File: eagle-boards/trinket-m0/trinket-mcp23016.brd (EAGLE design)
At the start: 60 x 41.6 mm, 10 parts, among them IC1 MCP23016P, Q1 BC547

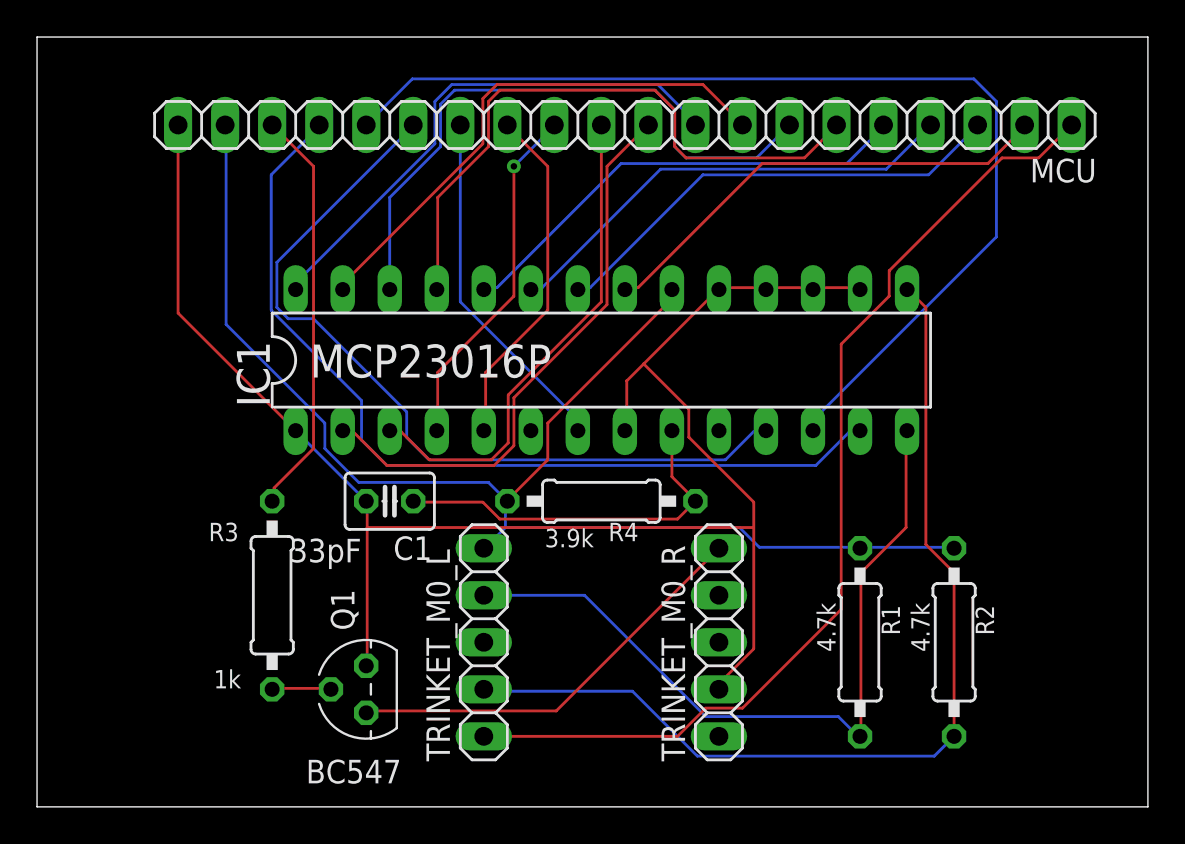
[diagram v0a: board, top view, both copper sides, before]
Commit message: Clean up the Trinket M0 based boards.
This makes the two board use the same size, and the same positioning of the common components.

It also reorients the silkscreen markings on the back to have the same orientation as the actuator board.

Also mark the used lines from the Trinket, as you can technically use any other MCU that can drive I²C.
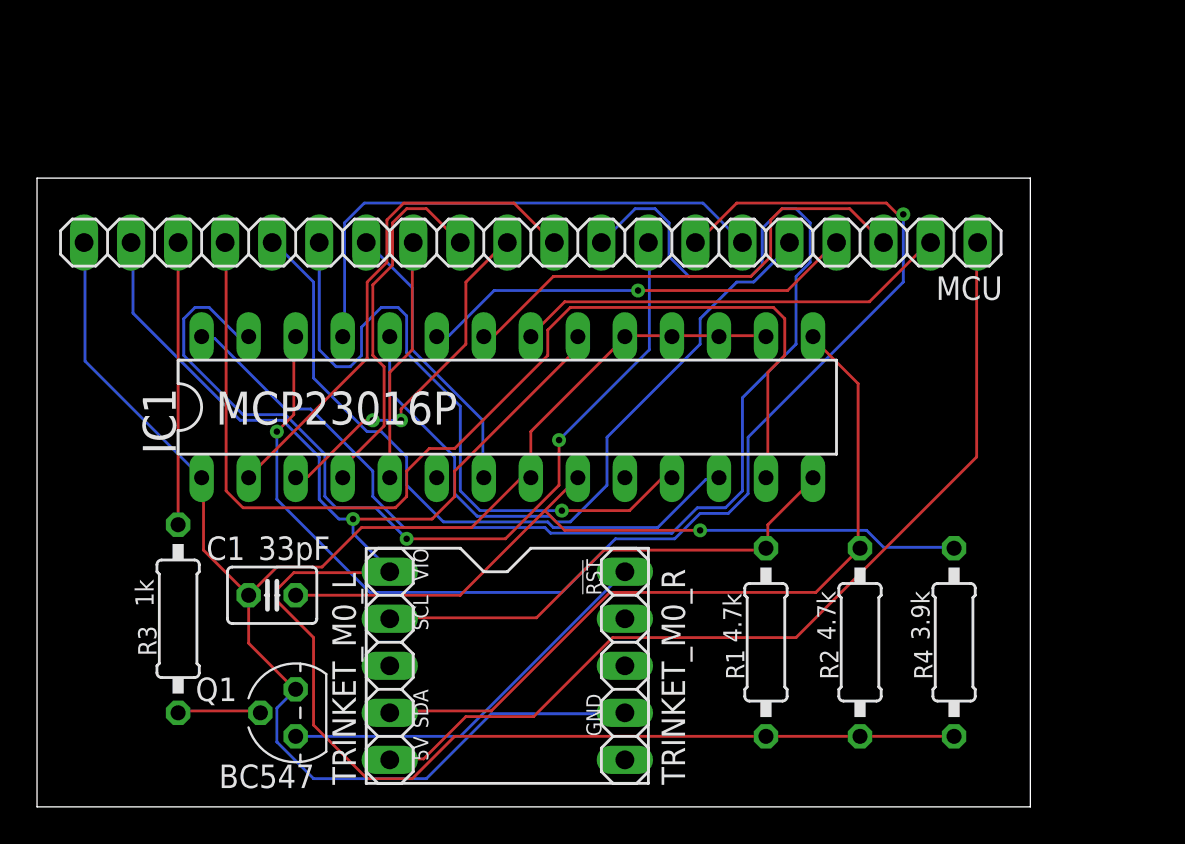
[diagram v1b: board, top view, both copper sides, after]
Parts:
- moved R4 20.5 mm to (49.5, 8.89), turned to 270 degrees
- moved C1 8.13 mm to (12.7, 11.4)
- moved MCU 8.13 mm to (26.7, 30.5)
- moved IC1 5.68 mm to (25.4, 21.6)
- moved R3 5.24 mm to (7.62, 10.2)
- moved TRINKET_M0_L 5.24 mm to (19.1, 7.62)
- moved TRINKET_M0_R 5.24 mm to (31.8, 7.62)
- moved R1 5.08 mm to (39.4, 8.89), turned to 90 degrees
- moved R2 5.08 mm to (44.5, 8.89), turned to 90 degrees
- moved Q1 4.02 mm to (14.0, 5.08)
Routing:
- net N$8: track 28.8 -> 69.0 mm
- net N$6: track 33.7 -> 69.9 mm, vias 0 -> 2
- net N$15: track 57.5 -> 35.5 mm
- net +3V3: track 73.7 -> 94.2 mm, vias 0 -> 1
- net N$20: track 20.4 -> 40.8 mm, vias 0 -> 1
- net N$7: track 28.7 -> 48.5 mm, vias 0 -> 2
- net SCL: track 41.1 -> 26.8 mm
- net N$4: track 25.3 -> 37.4 mm
- net N$16: track 48.4 -> 59.4 mm
- net SDA: track 52.5 -> 41.6 mm
- net N$10: track 26.7 -> 19.0 mm, vias 0 -> 2
- net N$14: track 44.2 -> 36.6 mm, vias 0 -> 1
- net N$18: track 22.2 -> 15.2 mm
- net N$12: track 18.8 -> 13.3 mm
- net N$5: track 33.8 -> 29.0 mm
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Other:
- board size 60 x 41.6 mm -> 53.6 x 34 mm
- board text added: "!RST"
- board text added: "5V"
- board text added: "Birch Books Smart Home Controller Module Trinket M0 MCP23016 rev. 1b"
- board text added: "GND"
- board text added: "SCL"
- board text added: "SDA"
- board text added: "VIO"
- board text removed: "Birch Books Smart Home Controller Module Trinket M0 rev. 1a"
